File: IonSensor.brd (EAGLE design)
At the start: 50.8 x 22.9 mm, 44 parts, among them IC1 QUAD_OPAMPD, IC2 QUAD_OPAMPD, IC3 QUAD_OPAMPD, X1 B5B-XH-2

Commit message: Revert "Added JST XH Connector"
This reverts commit 28e9dc296f10d82968848f6f33b36970200c6171.
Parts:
- removed X1: B5B-XH-2, con-JST XH:B5B-XH-A
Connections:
- net CH0: no longer X1.4
- net CH1: no longer X1.3
- net CH2: no longer X1.2
- net GND: no longer X1.1
- net REF: no longer X1.5
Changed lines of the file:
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@@
 <attribute name="VALUE" x="36.068" y="18.669" size="1.27" layer="27" rot="R270"/>
-</element>
-<element name="X1" library="con-JST XH" package="B5B-XH-A" value="B5B-XH-2" x="46.99" y="11.43" smashed="yes" rot="R270">
-<attribute name="NAME" x="46.99" y="3.382" size="1.016" layer="25" rot="R180" align="bottom-center"/>
-<attribute name="VALUE" x="48.26" y="6.43" size="1.016" layer="27" rot="R270" align="bottom-right"/>
 </element>
 </elements>
@@
 <wire x1="24.13" y1="16.129" x2="24.13" y2="12.7" width="0.254" layer="16"/>
 <wire x1="36.83" y1="16.129" x2="36.83" y2="12.7" width="0.254" layer="16"/>
-<contactref element="X1" pad="1"/>
-<wire x1="38.1" y1="8.3566" x2="36.83" y2="12.7" width="0" layer="19" extent="1-1"/>
-<wire x1="38.1" y1="3.81" x2="38.1" y2="8.3566" width="0" layer="19" extent="1-1"/>
-<wire x1="41.925" y1="3.81" x2="43.18" y2="3.81" width="0" layer="19" extent="1-1"/>
-<wire x1="34.275" y1="3.81" x2="33.02" y2="3.81" width="0" layer="19" extent="1-1"/>
-<wire x1="30.48" y1="3.81" x2="33.02" y2="3.81" width="0" layer="19" extent="1-1"/>
-<wire x1="29.225" y1="3.81" x2="30.48" y2="3.81" width="0" layer="19" extent="1-1"/>
-<wire x1="21.575" y1="3.81" x2="20.32" y2="3.81" width="0" layer="19" extent="1-1"/>
-<wire x1="17.78" y1="3.81" x2="20.32" y2="3.81" width="0" layer="19" extent="1-1"/>
-<wire x1="16.525" y1="3.81" x2="17.78" y2="3.81" width="0" layer="19" extent="1-1"/>
-<wire x1="8.875" y1="3.81" x2="7.62" y2="3.81" width="0" layer="19" extent="1-1"/>
-<wire x1="25.4" y1="8.3566" x2="25.4" y2="3.81" width="0" layer="19" extent="1-1"/>
-<wire x1="24.13" y1="12.7" x2="25.4" y2="8.3566" width="0" layer="19" extent="1-1"/>
-<wire x1="12.7" y1="8.3566" x2="12.7" y2="3.81" width="0" layer="19" extent="1-1"/>
-<wire x1="11.43" y1="12.7" x2="12.7" y2="8.3566" width="0" layer="19" extent="1-1"/>
-<wire x1="46.99" y1="6.43" x2="7.62" y2="3.81" width="0" layer="19" extent="1-1"/>
 </signal>
 <signal name="+3V3">
@@
 <signal name="CH0">
 <contactref element="IC1" pad="3"/>
-<contactref element="X1" pad="4"/>
-<wire x1="46.99" y1="13.93" x2="13.97" y2="14.5034" width="0" layer="19" extent="1-1"/>
 </signal>
 <signal name="CH1">
 <contactref element="IC2" pad="3"/>
-<contactref element="X1" pad="3"/>
-<wire x1="46.99" y1="11.43" x2="26.67" y2="14.5034" width="0" layer="19" extent="1-1"/>
 </signal>
 <signal name="CH2">
 <contactref element="IC3" pad="3"/>
-<contactref element="X1" pad="2"/>
-<wire x1="46.99" y1="8.93" x2="39.37" y2="14.5034" width="0" layer="19" extent="1-1"/>
 </signal>
 <signal name="REF">
@@
 <contactref element="IC2" pad="5"/>
 <contactref element="IC3" pad="5"/>
-<contactref element="X1" pad="5"/>
 <wire x1="24.13" y1="14.5034" x2="36.83" y2="14.5034" width="0" layer="19" extent="1-1"/>
 <wire x1="11.43" y1="14.5034" x2="24.13" y2="14.5034" width="0" layer="19" extent="1-1"/>
-<wire x1="46.99" y1="16.43" x2="11.43" y2="14.5034" width="0" layer="19" extent="1-1"/>
 </signal>
 <signal name="C1+">

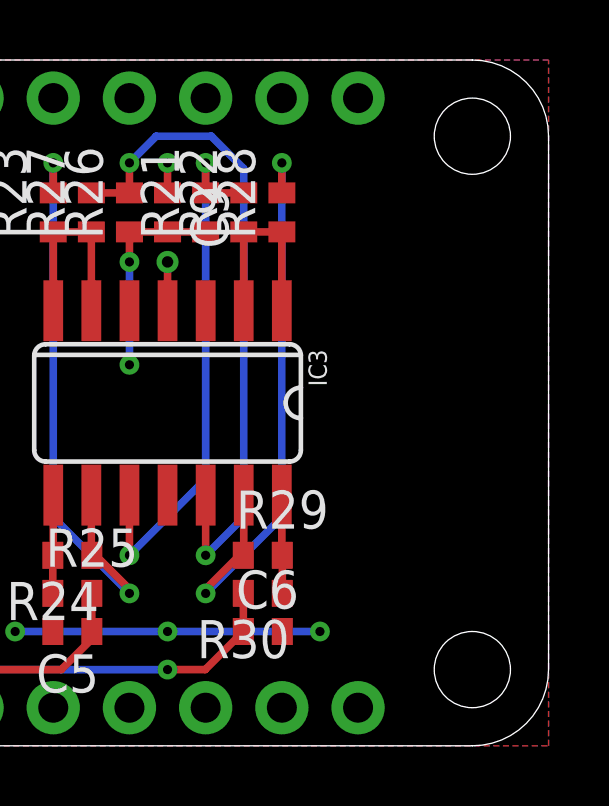
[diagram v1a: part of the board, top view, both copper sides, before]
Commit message: Added JST XH Connector
Added JST XH connector. TODO: Wire channels up!
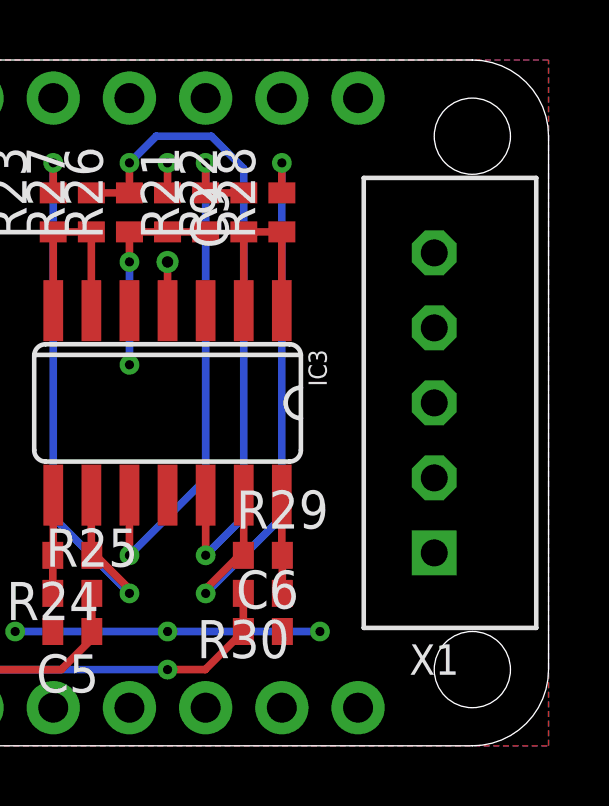
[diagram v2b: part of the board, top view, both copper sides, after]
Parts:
- added X1: B5B-XH-2, con-JST XH:B5B-XH-A
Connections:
- net CH0: now also X1.4
- net CH1: now also X1.3
- net CH2: now also X1.2
- net GND: now also X1.1
- net REF: now also X1.5
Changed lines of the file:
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@@
 <attribute name="VALUE" x="36.068" y="18.669" size="1.27" layer="27" rot="R270"/>
+</element>
+<element name="X1" library="con-JST XH" package="B5B-XH-A" value="B5B-XH-2" x="46.99" y="11.43" smashed="yes" rot="R270">
+<attribute name="NAME" x="46.99" y="3.382" size="1.016" layer="25" rot="R180" align="bottom-center"/>
+<attribute name="VALUE" x="48.26" y="6.43" size="1.016" layer="27" rot="R270" align="bottom-right"/>
 </element>
 </elements>
@@
 <wire x1="24.13" y1="16.129" x2="24.13" y2="12.7" width="0.254" layer="16"/>
 <wire x1="36.83" y1="16.129" x2="36.83" y2="12.7" width="0.254" layer="16"/>
+<contactref element="X1" pad="1"/>
+<wire x1="38.1" y1="8.3566" x2="36.83" y2="12.7" width="0" layer="19" extent="1-1"/>
+<wire x1="38.1" y1="3.81" x2="38.1" y2="8.3566" width="0" layer="19" extent="1-1"/>
+<wire x1="41.925" y1="3.81" x2="43.18" y2="3.81" width="0" layer="19" extent="1-1"/>
+<wire x1="34.275" y1="3.81" x2="33.02" y2="3.81" width="0" layer="19" extent="1-1"/>
+<wire x1="30.48" y1="3.81" x2="33.02" y2="3.81" width="0" layer="19" extent="1-1"/>
+<wire x1="29.225" y1="3.81" x2="30.48" y2="3.81" width="0" layer="19" extent="1-1"/>
+<wire x1="21.575" y1="3.81" x2="20.32" y2="3.81" width="0" layer="19" extent="1-1"/>
+<wire x1="17.78" y1="3.81" x2="20.32" y2="3.81" width="0" layer="19" extent="1-1"/>
+<wire x1="16.525" y1="3.81" x2="17.78" y2="3.81" width="0" layer="19" extent="1-1"/>
+<wire x1="8.875" y1="3.81" x2="7.62" y2="3.81" width="0" layer="19" extent="1-1"/>
+<wire x1="25.4" y1="8.3566" x2="25.4" y2="3.81" width="0" layer="19" extent="1-1"/>
+<wire x1="24.13" y1="12.7" x2="25.4" y2="8.3566" width="0" layer="19" extent="1-1"/>
+<wire x1="12.7" y1="8.3566" x2="12.7" y2="3.81" width="0" layer="19" extent="1-1"/>
+<wire x1="11.43" y1="12.7" x2="12.7" y2="8.3566" width="0" layer="19" extent="1-1"/>
+<wire x1="46.99" y1="6.43" x2="7.62" y2="3.81" width="0" layer="19" extent="1-1"/>
 </signal>
 <signal name="+3V3">
@@
 <signal name="CH0">
 <contactref element="IC1" pad="3"/>
+<contactref element="X1" pad="4"/>
+<wire x1="46.99" y1="13.93" x2="13.97" y2="14.5034" width="0" layer="19" extent="1-1"/>
 </signal>
 <signal name="CH1">
 <contactref element="IC2" pad="3"/>
+<contactref element="X1" pad="3"/>
+<wire x1="46.99" y1="11.43" x2="26.67" y2="14.5034" width="0" layer="19" extent="1-1"/>
 </signal>
 <signal name="CH2">
 <contactref element="IC3" pad="3"/>
+<contactref element="X1" pad="2"/>
+<wire x1="46.99" y1="8.93" x2="39.37" y2="14.5034" width="0" layer="19" extent="1-1"/>
 </signal>
 <signal name="REF">
@@
 <contactref element="IC2" pad="5"/>
 <contactref element="IC3" pad="5"/>
+<contactref element="X1" pad="5"/>
 <wire x1="24.13" y1="14.5034" x2="36.83" y2="14.5034" width="0" layer="19" extent="1-1"/>
 <wire x1="11.43" y1="14.5034" x2="24.13" y2="14.5034" width="0" layer="19" extent="1-1"/>
+<wire x1="46.99" y1="16.43" x2="11.43" y2="14.5034" width="0" layer="19" extent="1-1"/>
 </signal>
 <signal name="C1+">
